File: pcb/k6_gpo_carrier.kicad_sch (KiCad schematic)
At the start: 0 parts

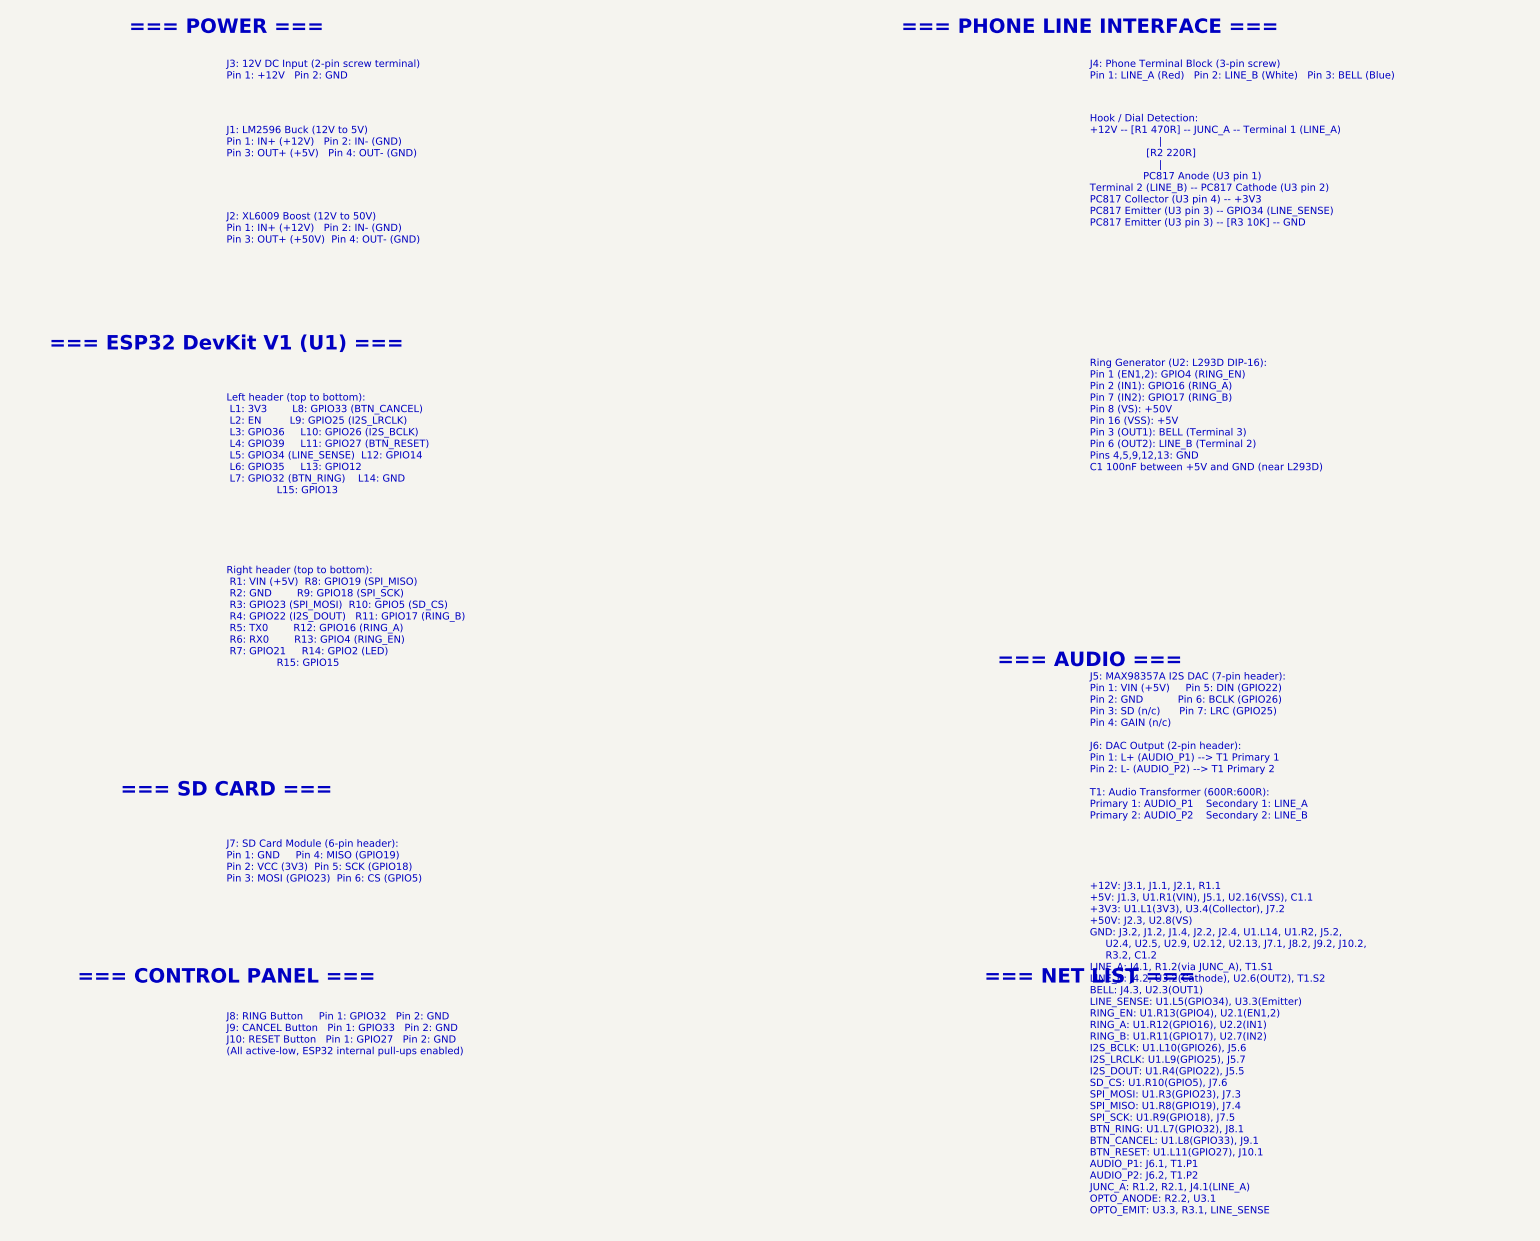
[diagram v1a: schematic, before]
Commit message: feat: Replace LM2596 module with TO-220-5 IC and full buck converter circuit
- U4: LM2596-5.0 TO-220-5 IC (VIN, SW_OUT, GND, FB, ON/OFF)
- C2: 680µF 25V input capacitor
- L1: 33µH power inductor (SW_OUT → +5V)
- D1: 1N5825 Schottky freewheeling diode
- C3: 220µF 25V output capacitor
- New SW_OUT net for switch node connections
- Dashed silkscreen clearance outlines for:
  - XL6009 boost module (43×21mm)
  - MAX98357A DAC module (19×18mm)
  - Micro-SD card module (25×20mm)
- J5/J6/T1/J4 moved down to avoid XL6009 module zone overlap
- PINOUT.md updated with full LM2596 circuit documentation
- Schematic netlist updated for new components

Co-Authored-By: Devin AI <158243242+devin-ai-integration[bot]@users.noreply.github.com>
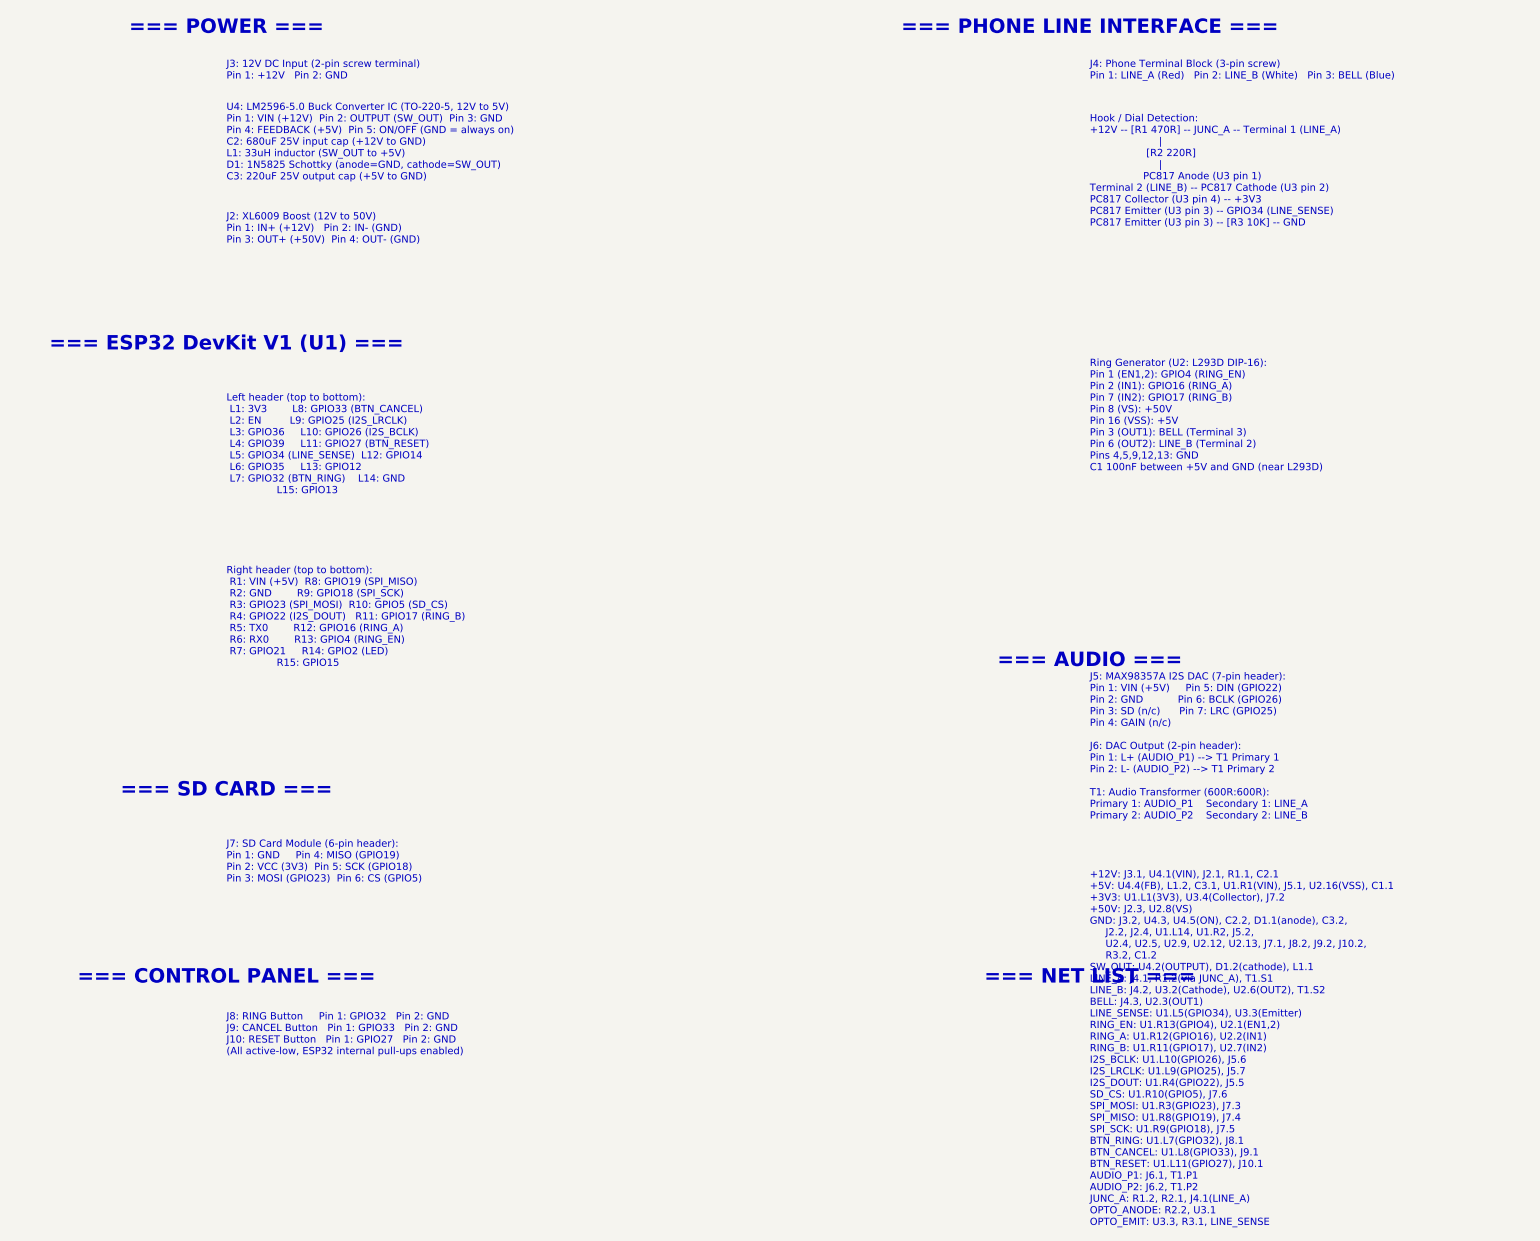
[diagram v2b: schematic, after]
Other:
- note added: "+12V: J3.1, U4.1(VIN), J2.1, R1.1, C2.1 +5V: U4.4(FB), L1.2, C3.1, U1.R1(VIN), J5.1, U2.16(VSS), C1.1 +3V3: U1.L1(3V3), U3.4(Collector), J7.2 +50V: J2.3, U2.8(VS) GND: J3.2, U4.3, U4.5(ON), C2.2, D1.1(anode), C3.2, J2.2, J2.4, U1.L14, U1.R2, J5.2, U2.4, U2.5, U2.9, U2.12, U2.13, J7.1, J8.2, J9.2, J10.2, R3.2, C1.2 SW_OUT: U4.2(OUTPUT), D1.2(cathode), L1.1 LINE_A: J4.1, R1.2(via JUNC_A), T1.S1 LIN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"
- note added: "U4: LM2596-5.0 Buck Converter IC (TO-220-5, 12V to 5V) Pin 1: VIN (+12V) Pin 2: OUTPUT (SW_OUT) Pin 3: GND Pin 4: FEEDBACK (+5V) Pin 5: ON/OFF (GND = always on) C2: 680uF 25V input cap (+12V to GND) L1: 33uH inductor (SW_OUT to +5V) D1: 1N5825 Schottky (anode=GND, cathode=SW_OUT) C3: 220uF 25V output cap (+5V to GND)"
- note removed: "+12V: J3.1, J1.1, J2.1, R1.1 +5V: J1.3, U1.R1(VIN), J5.1, U2.16(VSS), C1.1 +3V3: U1.L1(3V3), U3.4(Collector), J7.2 +50V: J2.3, U2.8(VS) GND: J3.2, J1.2, J1.4, J2.2, J2.4, U1.L14, U1.R2, J5.2, U2.4, U2.5, U2.9, U2.12, U2.13, J7.1, J8.2, J9.2, J10.2, R3.2, C1.2 LINE_A: J4.1, R1.2(via JUNC_A), T1.S1 LINE_B: J4.2, U3.2(Cathode), U2.6(OUT2), T1.S2 BELL: J4.3, U2.3(OUT1) LINE_SENSE: U1.L5(GPIO34), U3.3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"
- note removed: "J1: LM2596 Buck (12V to 5V) Pin 1: IN+ (+12V) Pin 2: IN- (GND) Pin 3: OUT+ (+5V) Pin 4: OUT- (GND)"
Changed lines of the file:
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@@
   (text "J3: 12V DC Input (2-pin screw terminal)\nPin 1: +12V   Pin 2: GND" (at 25.4 33.02 0)
     (effects (font (size 1.27 1.27)) (justify left)))
-  (text "J1: LM2596 Buck (12V to 5V)\nPin 1: IN+ (+12V)   Pin 2: IN- (GND)\nPin 3: OUT+ (+5V)   Pin 4: OUT- (GND)" (at 25.4 45.72 0)
+  (text "U4: LM2596-5.0 Buck Converter IC (TO-220-5, 12V to 5V)\nPin 1: VIN (+12V)  Pin 2: OUTPUT (SW_OUT)  Pin 3: GND\nPin 4: FEEDBACK (+5V)  Pin 5: ON/OFF (GND = always on)\nC2: 680uF 25V input cap (+12V to GND)\nL1: 33uH inductor (SW_OUT to +5V)\nD1: 1N5825 Schottky (anode=GND, cathode=SW_OUT)\nC3: 220uF 25V output cap (+5V to GND)" (at 25.4 45.72 0)
     (effects (font (size 1.27 1.27)) (justify left)))
   (text "J2: XL6009 Boost (12V to 50V)\nPin 1: IN+ (+12V)   Pin 2: IN- (GND)\nPin 3: OUT+ (+50V)  Pin 4: OUT- (GND)" (at 25.4 60.96 0)
@@
   (text "=== NET LIST ===" (at 177.8 193.04 0)
     (effects (font (size 2.54 2.54) (bold yes))))
-  (text "+12V: J3.1, J1.1, J2.1, R1.1\n+5V: J1.3, U1.R1(VIN), J5.1, U2.16(VSS), C1.1\n+3V3: U1.L1(3V3), U3.4(Collector), J7.2\n+50V: J2.3, U2.8(VS)\nGND: J3.2, J1.2, J1.4, J2.2, J2.4, U1.L14, U1.R2, J5.2,\n     U2.4, U2.5, U2.9, U2.12, U2.13, J7.1, J8.2, J9.2, J10.2,\n     R3.2, C1.2\nLINE_A: J4.1, R1.2(via JUNC_A), T1.S1\nLINE_B: J4.2, U3.2(Cathode), U2.6(OUT2), T1.S2\nBELL: J4.3, U2.3(OUT1)\nLINE_SENSE: U1.L5(GPIO34), U3.3(Emitter)\nRING_EN: U1.R13(GPIO4), U2.1(EN1,2)\nRING_A: U1.R12(GPIO16), U2.2(IN1)\nRING_B: U1.R11(GPIO17), U2.7(IN2)\nI2S_BCLK: U1.L10(GPIO26), J5.6\nI2S_LRCLK: U1.L9(GPIO25), J5.7\nI2S_DOUT: U1.R4(GPIO22), J5.5\nSD_CS: U1.R10(GPIO5), J7.6\nSPI_MOSI: U1.R3(GPIO23), J7.3\nSPI_MISO: U1.R8(GPIO19), J7.4\nSPI_SCK: U1.R9(GPIO18), J7.5\nBTN_RING: U1.L7(GPIO32), J8.1\nBTN_CANCEL: U1.L8(GPIO33), J9.1\nBTN_RESET: U1.L11(GPIO27), J10.1\nAUDIO_P1: J6.1, T1.P1\nAUDIO_P2: J6.2, T1.P2\nJUNC_A: R1.2, R2.1, J4.1(LINE_A)\nOPTO_ANODE: R2.2, U3.1\nOPTO_EMIT: U3.3, R3.1, LINE_SENSE" (at 177.8 205.74 0)
+  (text "+12V: J3.1, U4.1(VIN), J2.1, R1.1, C2.1\n+5V: U4.4(FB), L1.2, C3.1, U1.R1(VIN), J5.1, U2.16(VSS), C1.1\n+3V3: U1.L1(3V3), U3.4(Collector), J7.2\n+50V: J2.3, U2.8(VS)\nGND: J3.2, U4.3, U4.5(ON), C2.2, D1.1(anode), C3.2,\n     J2.2, J2.4, U1.L14, U1.R2, J5.2,\n     U2.4, U2.5, U2.9, U2.12, U2.13, J7.1, J8.2, J9.2, J10.2,\n     R3.2, C1.2\nSW_OUT: U4.2(OUTPUT), D1.2(cathode), L1.1\nLINE_A: J4.1, R1.2(via JUNC_A), T1.S1\nLINE_B: J4.2, U3.2(Cathode), U2.6(OUT2), T1.S2\nBELL: J4.3, U2.3(OUT1)\nLINE_SENSE: U1.L5(GPIO34), U3.3(Emitter)\nRING_EN: U1.R13(GPIO4), U2.1(EN1,2)\nRING_A: U1.R12(GPIO16), U2.2(IN1)\nRING_B: U1.R11(GPIO17), U2.7(IN2)\nI2S_BCLK: U1.L10(GPIO26), J5.6\nI2S_LRCLK: U1.L9(GPIO25), J5.7\nI2S_DOUT: U1.R4(GPIO22), J5.5\nSD_CS: U1.R10(GPIO5), J7.6\nSPI_MOSI: U1.R3(GPIO23), J7.3\nSPI_MISO: U1.R8(GPIO19), J7.4\nSPI_SCK: U1.R9(GPIO18), J7.5\nBTN_RING: U1.L7(GPIO32), J8.1\nBTN_CANCEL: U1.L8(GPIO33), J9.1\nBTN_RESET: U1.L11(GPIO27), J10.1\nAUDIO_P1: J6.1, T1.P1\nAUDIO_P2: J6.2, T1.P2\nJUNC_A: R1.2, R2.1, J4.1(LINE_A)\nOPTO_ANODE: R2.2, U3.1\nOPTO_EMIT: U3.3, R3.1, LINE_SENSE" (at 177.8 205.74 0)
     (effects (font (size 1.27 1.27)) (justify left)))
 )
